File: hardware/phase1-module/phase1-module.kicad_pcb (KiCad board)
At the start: 4 copper layers, 120 x 80 mm, 144 parts, among them J1 VBUS IN, J2 SWD, J3 UART, J4 OUTPUT, J5 BACKPLANE, J6 FAN, Q1 CSD18563Q5A, Q2 CSD18563Q5A, Q3 60V NFET, Q4 60V NFET, Q5 2N7002, Q6 2N7002, Q7 2N7002, Q8 2N7002, Q9 2N7002, U1 DAC80502DRXT, U10 STM32G431CBT6, U11 TCAN1042HGV, U2 OPA2333, U3 LM5145RGYR, U4 INA240A3, U5 INA228, U6 LTC7004, U7 TLV7011, U8 LMR36015AQRNXRQ1, U9 NCP1117-3.3, Y1 8MHz

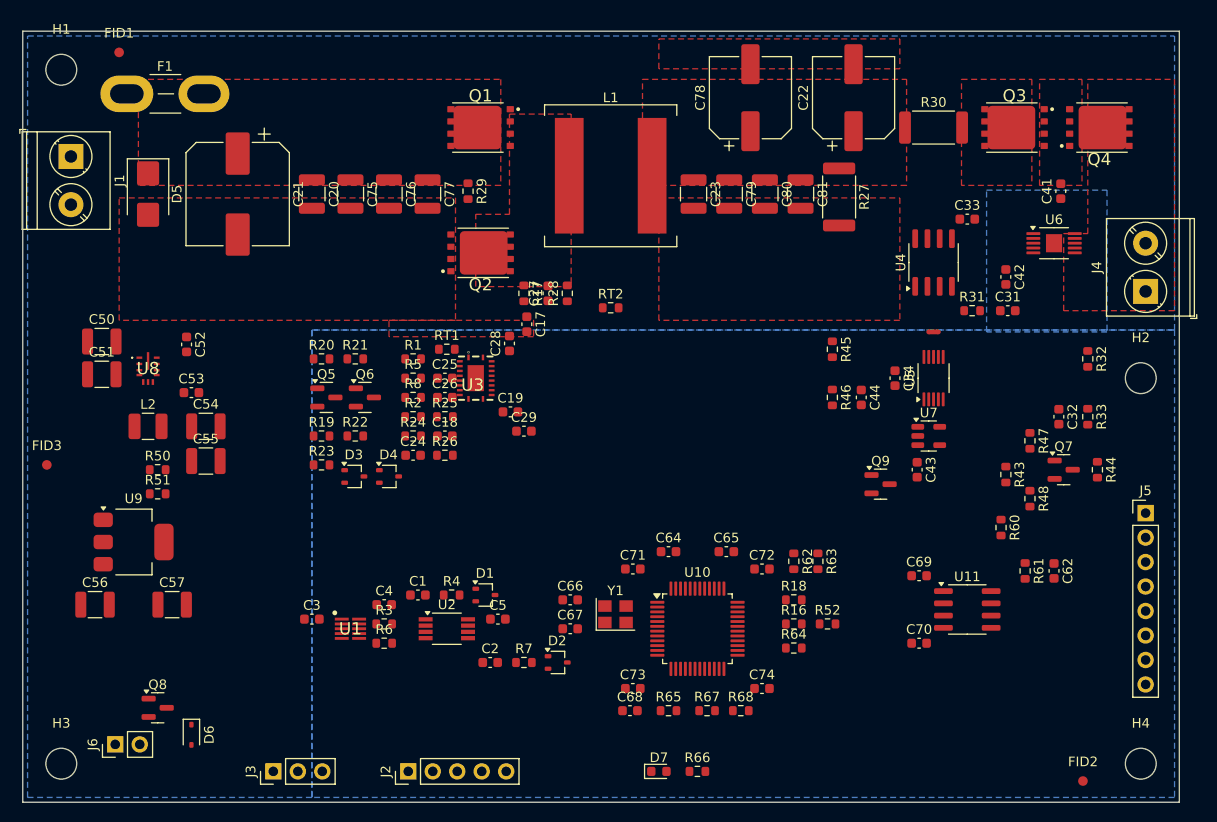
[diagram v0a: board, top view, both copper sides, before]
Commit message: Routing pass 1: power copper, vias, critical routes — 0 copper DRC violations
route_board.py (deterministic pass after gen_board.py):
- In2.Cu same-net heat patches under all six F.Cu power pours; thermal via
  arrays on Q1-Q4 tabs and L1 pads (heat + current into the inner layer)
- EP vias (LM5145, LTC7004), NT1 star-tie vias, J1/J4 PGND clusters,
  PGND_TOP/bar plane ties, 86 seam-aware power-pad vias (plane checked at
  the via position, dedup against existing same-net vias), 63 stitches
- critical routes: true-Kelvin sense pair (shunt inner edges -> INA240 ->
  INA228, routed around the amp, 0.24-0.3mm), LM5145 right-column fan-out
  (0.5mm pitch escapes at exact-clearance widths), HO/LO gate runs on B.Cu,
  BST, ILIM, VIN corridor, snubber, VBUS input link, aux VBUS_F trunk,
  3V3 trunk to the In2 zone
- C28 relocated into the PGND bar, C19 tap directly on the ILIM track,
  NT1 moved out of the sense corridor, C33 clear of the sense jog

SPICE (ngspice, kicad-happy spice skill): 38 pass / 1 warn / 0 fail —
all dividers, comp poles, PDN and both regulator FB dividers confirm
doc-06 math; crystal warn -> order 8MHz part with CL=8pF (manifest note).
Web-verified Coilcraft Doc373: XAL1350-103 Isat ~18A @30% drop, DCR
~8.7mOhm (manifest said 28A — fixed). DRC: 0 clearance/hole/dangling;
187 unconnected pads remain for the signal autoroute pass.

Co-Authored-By: Claude Fable 5 <noreply@anthropic.com>
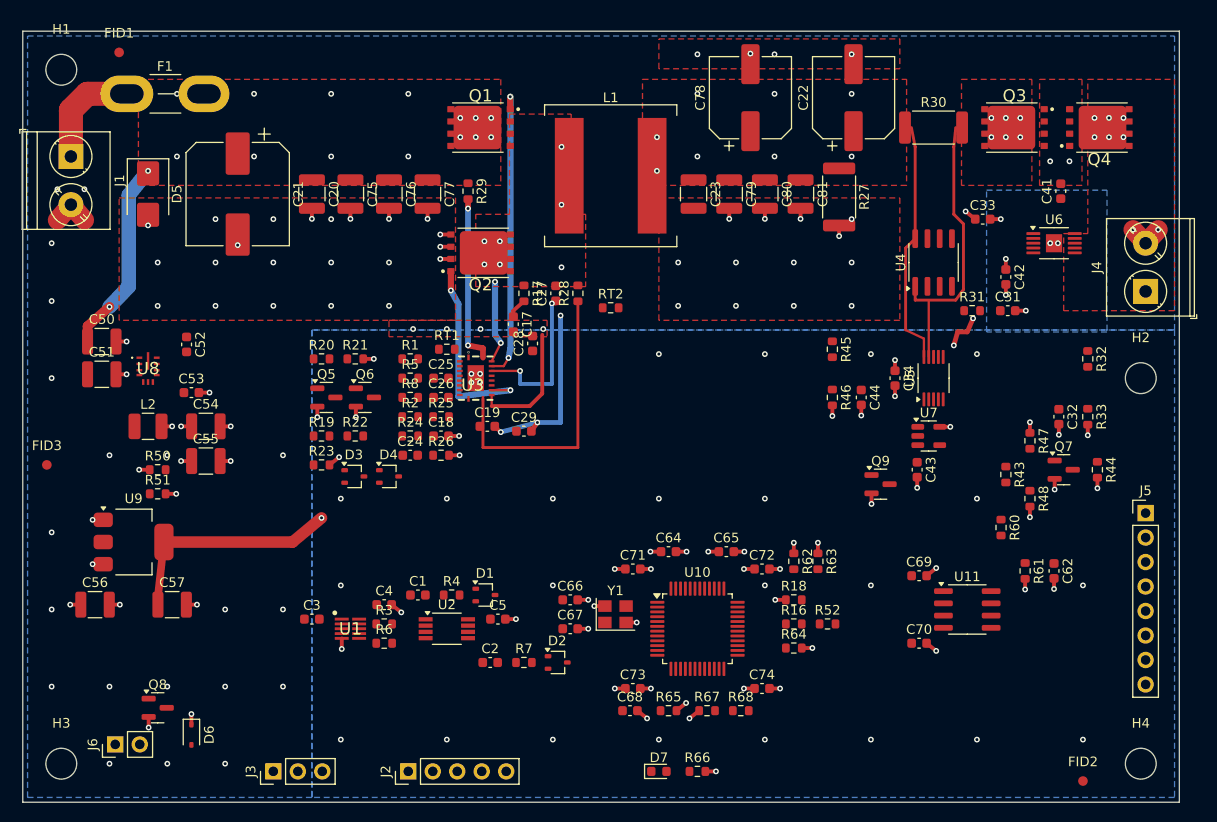
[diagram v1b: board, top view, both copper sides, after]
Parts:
- moved NT1 3.00 mm to (117.5, 51.2)
- moved C19 2.83 mm to (68.2, 61.0)
- moved C28 2.40 mm to (72.9, 52.4)
- moved C33 1.60 mm to (119.6, 39.5)
- moved C17 1.40 mm to (70.9, 50.4)
- moved R28 1.10 mm to (77.6, 47.2)
- moved C27 0.80 mm to (75.3, 47.2)
- moved C18 0.40 mm to (63.4, 62.0)
- moved C25 0.40 mm to (63.4, 56.0)
- moved C26 0.40 mm to (63.4, 58.0)
- moved R25 0.40 mm to (63.4, 60.0)
- moved R26 0.40 mm to (63.4, 64.0)
- moved C24 0.30 mm to (60.2, 64.0)
- moved R1 0.30 mm to (60.2, 54.0)
- moved R2 0.30 mm to (60.2, 60.0)
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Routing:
- net PGND: track 0.00 -> 68.5 mm, vias 0 -> 79
- net AGND: track 0.00 -> 45.4 mm, vias 0 -> 69
- net 3V3: track 0.00 -> 38.3 mm, vias 0 -> 14
- net HO_G: track 0.00 -> 30.7 mm, vias 0 -> 2
- net VOUT_SW: track 0.00 -> 30.1 mm, vias 0 -> 6
- net PS_ILIM: track 0.00 -> 29.9 mm
- net VOUT_INT: track 0.00 -> 25.5 mm, vias 0 -> 8
- net LO_G: track 0.00 -> 20.6 mm, vias 0 -> 2
- net VBUS_F: track 0.00 -> 20.2 mm, vias 0 -> 16
- net PS_VIN: track 0.00 -> 17.5 mm, vias 0 -> 2
- net PS_BST: track 0.00 -> 16.3 mm, vias 0 -> 2
- net VBUS: track 0.00 -> 11.3 mm
- net 5V0: track 0.00 -> 11.2 mm, vias 0 -> 10
- net SW: track 0.00 -> 8.66 mm, vias 0 -> 9
- net SNUB: track 0.00 -> 2.05 mm
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- added copper zone on In2.Cu, net DISC_SRC
- added copper zone on In2.Cu, net SW
- added copper zone on In2.Cu, net VBUS_F
- added copper zone on In2.Cu, net VOUT
- added copper zone on In2.Cu, net VOUT_INT
- added copper zone on In2.Cu, net VOUT_SW

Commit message: Backplane fab-ready; DRC "benign bookkeeping" was two real bugs
The lib_footprint_issues class everyone has been waving through (39
backplane, 180 phase-2, 144 phase-1) was never one thing, and neither
half was harmless bookkeeping:

 1. The board generators add footprints by name only, leaving the FPID
    library nickname empty. common/fix_fpids.py resolves each item name
    against the project library first, then the system libraries, and
    writes the nickname back (363 resolved across three boards, none
    guessed — unresolved names are reported, never invented).
 2. KiCad's global fp-lib-table expands ${KICAD7_FOOTPRINT_DIR}, which
    only the GUI sets. Headless DRC could not expand a single library
    URI, so every footprint came back "not found in library". Every
    run_drc.py now sets it before importing pcbnew.

Both mattered beyond noise: with the libraries unresolved, KiCad cannot
diff a board footprint against its library, so silent land-pattern drift
would pass unnoticed — and this project already caught one such bug in
LM5143 by hand.

    phase3-backplane   40 -> 0 violations, 0 unconnected
    phase2-module     191 -> 11 (silk only), 83 unconnected
    phase1-module     247 -> 75 (silk only)

phase3-backplane is now FAB-READY: silk reflowed (39/39 refs clean), no
plane islands, gerbers + drills plotted and cross-checked — Edge_Cuts
exactly 330.00 x 100.00 mm, drills 2x6.4mm (M6 entry lugs), 16x2.8mm
(8 slots x 2 XT60 pins), 6x3.2mm (M3), 86x1.0mm, 61x0.4mm.

New shared tooling in hardware/common (was phase-2-only, now serves every
board): layout_qa.py (silk reflow, PS-002 islands, gerber/drill plot with
the layer set read from the board) and finish_board.py as its CLI.

Correction: phase-1 is 187 unconnected, not the 33 in HANDOVER — that
figure came from an autoroute run that was never committed, and its
gitignored drc-report.txt kept showing the stale number. Verified against
the committed board.

Co-Authored-By: Claude Fable 5 <noreply@anth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
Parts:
- C1, C17, C18, C19, C2, C24, C25, C26, C27, C28, C29, C3, C31, C32, C33, C34, C4, C41, C42, C43, C44, C5, C52, C53, C62, C64, C65, C66, C67, C68, C69, C70, C71, C72, C73, C74: footprint C_0603_1608Metric -> Capacitor_SMD:C_0603_1608Metric
- C20, C23, C50, C51, C54, C55, C56, C57, C75, C76, C77, C79, C80, C81: footprint C_1210_3225Metric -> Capacitor_SMD:C_1210_3225Metric
- C21: footprint CP_Elec_10x10.5 -> Capacitor_SMD:CP_Elec_10x10.5
- C22, C78: footprint CP_Elec_8x11.9 -> Capacitor_SMD:CP_Elec_8x11.9
- D1, D2, D3, D4: footprint SOT-323_SC-70 -> Package_TO_SOT_SMD:SOT-323_SC-70
- D5: footprint D_SMB -> Diode_SMD:D_SMB
- D6: footprint D_SOD-323 -> Diode_SMD:D_SOD-323
- D7: footprint LED_0603_1608Metric -> LED_SMD:LED_0603_1608Metric
- F1: footprint Fuse_Blade_Mini_directSolder -> Fuse:Fuse_Blade_Mini_directSolder
- FID1, FID2, FID3: footprint Fiducial_1mm_Mask2mm -> Fiducial:Fiducial_1mm_Mask2mm
- H1, H2, H3, H4: footprint MountingHole_3.2mm_M3 -> MountingHole:MountingHole_3.2mm_M3
- J1, J4: footprint TerminalBlock_Phoenix_PT-1,5-2-5.0-H_1x02_P5.00mm_Horizontal -> TerminalBlock_Phoenix:TerminalBlock_Phoenix_PT-1,5-2-5.0-H_1x02_P5.00mm_Horizontal
- J2: footprint PinHeader_1x05_P2.54mm_Vertical -> Connector_PinHeader_2.54mm:PinHeader_1x05_P2.54mm_Vertical
- J3: footprint PinHeader_1x03_P2.54mm_Vertical -> Connector_PinHeader_2.54mm:PinHeader_1x03_P2.54mm_Vertical
- J5: footprint PinHeader_1x08_P2.54mm_Vertical -> Connector_PinHeader_2.54mm:PinHeader_1x08_P2.54mm_Vertical
- J6: footprint PinHeader_1x02_P2.54mm_Vertical -> Connector_PinHeader_2.54mm:PinHeader_1x02_P2.54mm_Vertical
- L1: footprint L_Coilcraft_XAL1350-XXX -> Inductor_SMD:L_Coilcraft_XAL1350-XXX
- L2: footprint L_1210_3225Metric -> Inductor_SMD:L_1210_3225Metric
- NT1: footprint NetTie-2_SMD_Pad0.5mm -> NetTie:NetTie-2_SMD_Pad0.5mm
- Q1, Q2, Q3, Q4: footprint PowerFET_SON5x6_GDS -> labbench:PowerFET_SON5x6_GDS
- Q5, Q6, Q7, Q8, Q9: footprint SOT-23 -> Package_TO_SOT_SMD:SOT-23
- R1, R16, R17, R18, R19, R2, R20, R21, R22, R23, R24, R25, R26, R28, R29, R3, R31, R32, R33, R4, R43, R44, R45, R46, R47, R48, R5, R50, R51, R52, R6, R60, R61, R62, R63, R64, R65, R66, R67, R68, R7, R8, RT1, RT2: footprint R_0603_1608Metric -> Resistor_SMD:R_0603_1608Metric
- R27, R30: footprint R_2512_6332Metric -> Resistor_SMD:R_2512_6332Metric
- U1: footprint DAC80502_DRX_WSON-10 -> labbench:DAC80502_DRX_WSON-10
- U10: footprint LQFP-48_7x7mm_P0.5mm -> Package_QFP:LQFP-48_7x7mm_P0.5mm
- U11, U4: footprint SOIC-8_3.9x4.9mm_P1.27mm -> Package_SO:SOIC-8_3.9x4.9mm_P1.27mm
- U2: footprint VSSOP-8_3.0x3.0mm_P0.65mm -> Package_SO:VSSOP-8_3.0x3.0mm_P0.65mm
- U3: footprint LM5145_RGY0020B -> labbench:LM5145_RGY0020B
- U5: footprint VSSOP-10_3x3mm_P0.5mm -> Package_SO:VSSOP-10_3x3mm_P0.5mm
- U6: footprint MSOP-10-1EP_3x3mm_P0.5mm_EP1.68x1.88mm -> Package_SO:MSOP-10-1EP_3x3mm_P0.5mm_EP1.68x1.88mm
- U7: footprint SOT-23-5 -> Package_TO_SOT_SMD:SOT-23-5
- U8: footprint LMR36015_RNX_VQFN-HR-12 -> labbench:LMR36015_RNX_VQFN-HR-12
- U9: footprint SOT-223-3_TabPin2 -> Package_TO_SOT_SMD:SOT-223-3_TabPin2
- Y1: footprint Crystal_SMD_3225-4Pin_3.2x2.5mm -> Crystal:Crystal_SMD_3225-4Pin_3.2x2.5mm

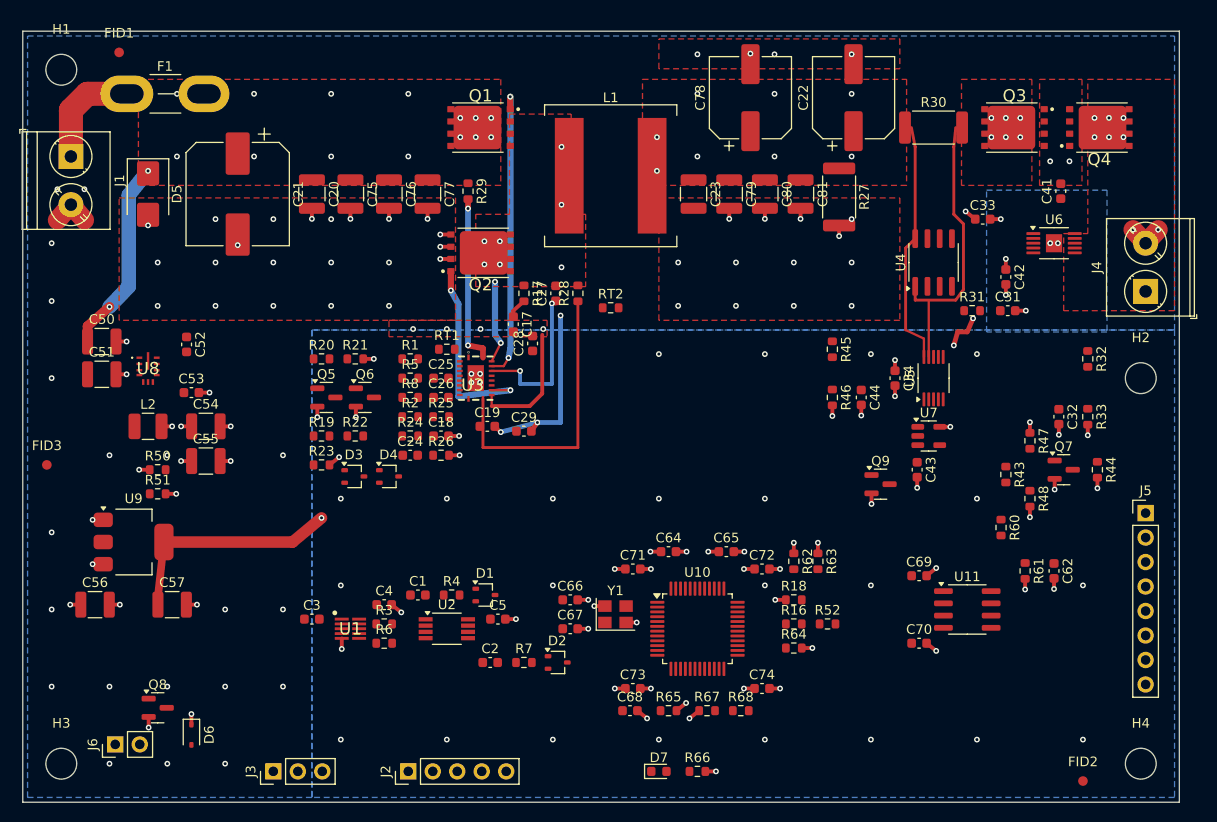
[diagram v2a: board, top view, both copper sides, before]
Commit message: Phase-1 module board: finish routing (187 -> 0 unconnected), fab zip
Routes every remaining connection of the 150 W module board with a
scripted chain on top of the pass-1 copper:

- fanout.py: placement nudges (C25, C26, R3, R6), hand escapes for
  U3's boxed-in SS/FPWM/FB pins, via drops for plane-net pads, and a
  solid zone join for J2.5 (starved thermal at the board edge)
- export_dsn.py / import_ses.py: Freerouting 1.9 round trip with the
  In1/In2 planes as power layers and F.Cu pours as keepouts
- finish_routes.py: exact-geometry A* router with rip-up that closes
  the connections Freerouting leaves open

DRC: 0 unconnected, 0 errors, 9 silk warnings. The fab zip (gerbers +
drill) is force-added despite the fab gitignore so the PR carries it.
HANDOVER.md and tools/README.md record the pipeline and the caveats.

Co-Authored-By: Claude Opus 5.5 (1M context) <noreply@anthropic.com>
Claude-Session: https://claude.ai/code/session_017ZrT5TjsLMQoxTZy1jabew
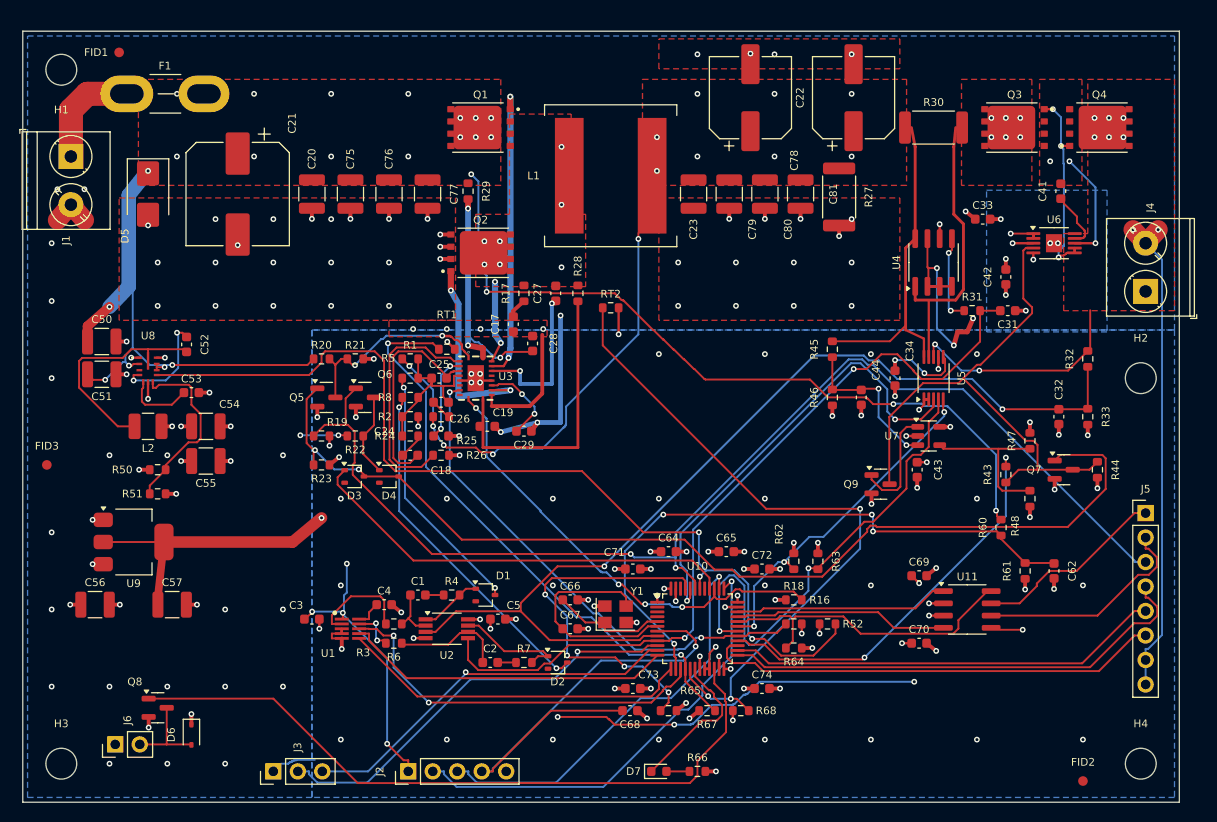
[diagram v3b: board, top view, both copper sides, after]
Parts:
- moved R3 1.00 mm to (58.5, 81.5)
- moved R6 1.00 mm to (58.5, 83.5)
- moved C26 0.50 mm to (63.4, 58.5)
- moved C25 0.20 mm to (63.2, 56.0)
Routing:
- net HW_EN: track 0.00 -> 122.9 mm, vias 0 -> 2
- net VBUS_F: track 20.2 -> 135.8 mm, vias 16 -> 24
- net EN_KILL: track 0.00 -> 109.4 mm, vias 0 -> 2
- net V_MEAS: track 0.00 -> 103.4 mm, vias 0 -> 2
- net AUX_PG: track 0.00 -> 100.1 mm, vias 0 -> 3
- net I_MEAS: track 0.00 -> 83.5 mm, vias 0 -> 2
- net FAN_PWM: track 0.00 -> 73.7 mm
- net NTC_IND: track 0.00 -> 71.3 mm, vias 0 -> 3
- net VBUS_SNS: track 0.00 -> 63.7 mm, vias 0 -> 4
- net NTC_FET: track 0.00 -> 61.8 mm, vias 0 -> 2
- net DISC_INP: track 0.00 -> 57.8 mm
- net VOUT_INT: track 25.5 -> 82.5 mm, vias 8 -> 13
- net 3V3: track 38.3 -> 92.2 mm, vias 14 -> 28
- net 5V0: track 11.2 -> 64.8 mm, vias 10 -> 22
- net PS_FPWM: track 0.00 -> 52.8 mm, vias 0 -> 2
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
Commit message: Phase-1 board: fix the three routing review items
- C28 (PS_VIN 100n) moved onto U3 pin 20: pad 1 lands on the PS_VIN
  feed 0.85 mm from the pin, pad 2 in the PGND bar beside a PGND via.
  PS_VIN copper 24.8 -> 17.7 mm.
- VBUS divider R60/R61/C62 moved from the far right edge to beside
  U10.14 (ADC), so the long run is the low-impedance VBUS_F side and
  C62 filters next to the pin. High-impedance VBUS_SNS copper
  63.7 -> 19.3 mm; the VBUS_F feed to R60 is 79 -> 61 mm.
- VOUT_INT FB sense run left as routed: 5.5 mm or more from SW copper
  on every layer, and its long end is the output side of the divider.
- All part offsets folded into gen_board.py PLACEMENT (C25, C26, R3,
  R6 from the first pass, plus the moves above); fanout.py NUDGES is
  now empty. PLACEMENT matches every footprint on the board.

New eco_move.py moves parts on the routed board and peels their old
routes; finish_routes.py gains a fallback that joins the other islands
first when the largest one is boxed in.

DRC: 0 unconnected, 0 errors, same 9 silk warnings. Fab zip regenerated.

Co-Authored-By: Claude Opus 5.5 (1M context) <noreply@anthropic.com>
Claude-Session: https://claude.ai/code/session_017ZrT5TjsLMQoxTZy1jabew
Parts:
- moved C62 43.9 mm to (86.5, 93.0), turned to 0 degrees
- moved R60 43.7 mm to (83.5, 93.0), turned to 0 degrees
- moved R61 43.3 mm to (85.0, 94.8), turned to 0 degrees
- moved C28 5.15 mm to (67.8, 52.2)
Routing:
- net VBUS_SNS: track 63.7 -> 19.3 mm, vias 4 -> 2
- net VBUS_F: track 135.8 -> 117.4 mm, vias 24 -> 25
- net PS_VIN: track 24.8 -> 17.7 mm, vias 3 -> 2
- net PGND: track 119.4 -> 115.0 mm
- net AGND: track 96.9 -> 95.9 mm, vias 87 -> 88
